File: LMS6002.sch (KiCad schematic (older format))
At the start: 40 parts, among them J1 SMA_H, J2 SMA_H, T1 B0322J5050, T2 B0322J5050, U3 LMS6002DR2

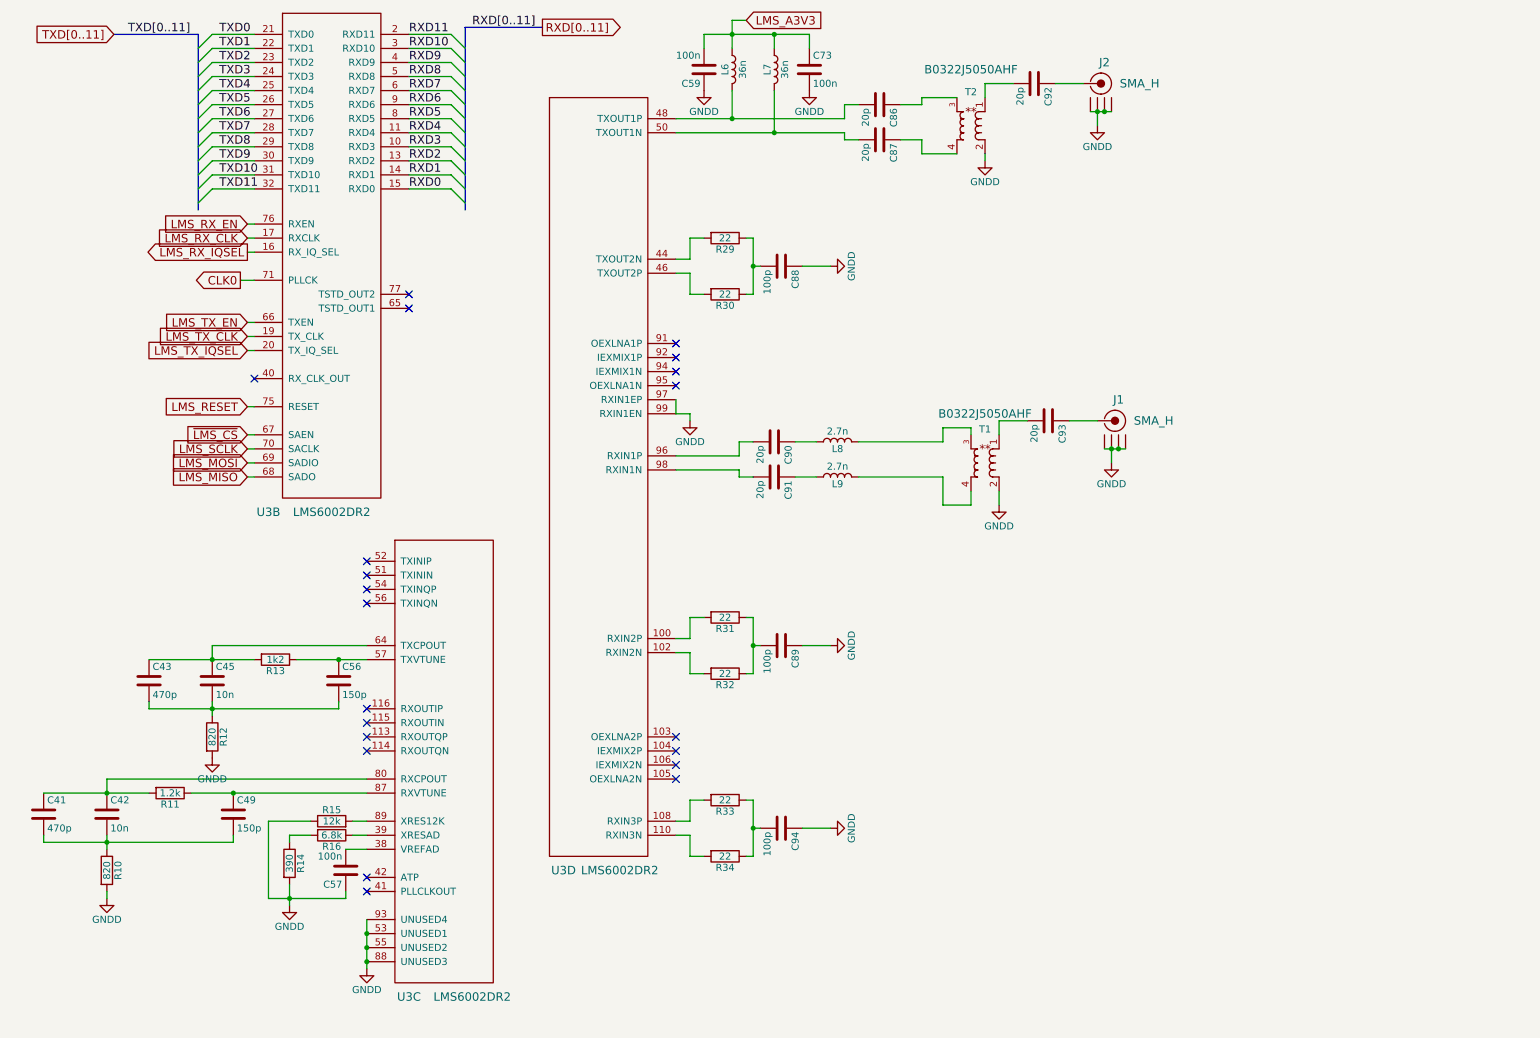
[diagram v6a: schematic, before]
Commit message: Changed RF sheet to add second path to TX and RX
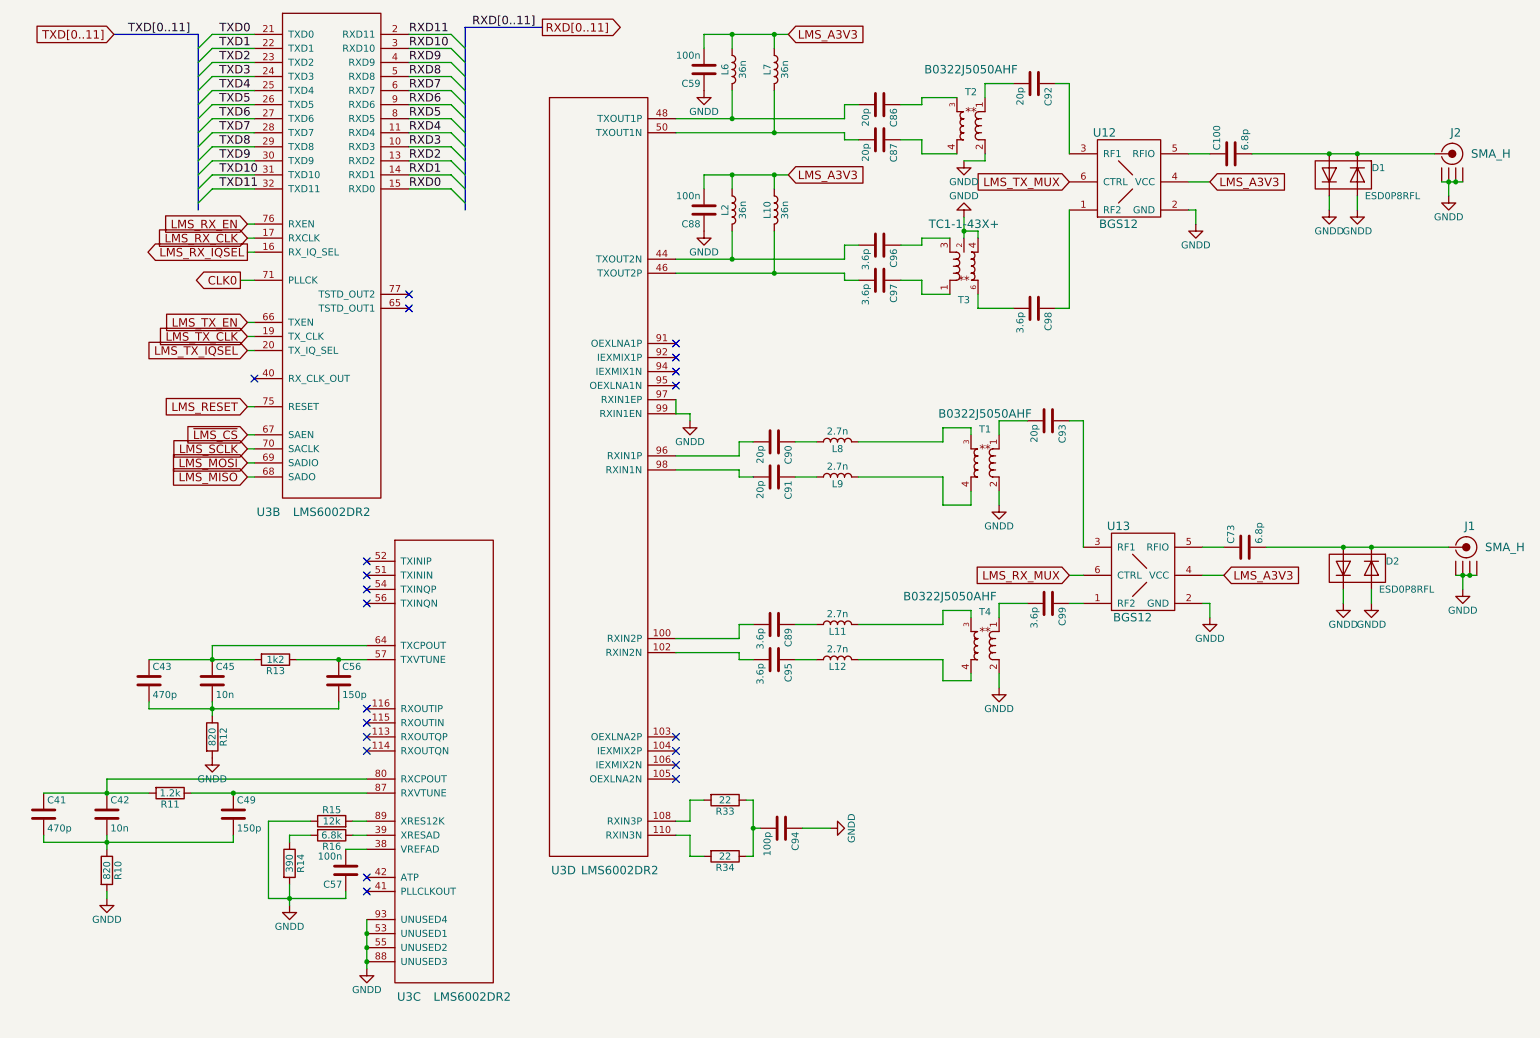
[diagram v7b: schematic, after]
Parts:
- removed R29, R30, R31, R32: 22, Resistors_SMD:R_0603, symbol R
- added C100: 6.8p, Capacitors_SMD:C_0603, symbol C
- added C95, C96, C97, C98, C99: 3.6p, Capacitors_SMD:C_0603, symbol C
- added D1, D2: ESD0P8RFL, sdr-foots:TSLP-4-7, symbol DualDiode
- added L10, L2: 36n, Inductors_SMD:L_0603, symbol L
- added L11, L12: 2.7n, Inductors_SMD:L_0603, symbol L
- added T3: TR_TC1-1-43X+, sdr-foots:TC1-1-43X+, symbol TR_TC1-1-43X+
- added T4: B0322J5050, sdr-foots:B0322J5050, symbol B0322J5050
- added U12, U13: BGS12, sdr-foots:TSLP-6-4, symbol BGS12
- C73: value 100n -> 6.8p
- C88: value 100p -> 100n
- C89: value 100p -> 3.6p
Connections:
- net GNDD: now also D1.2 (A), D1.3 (K), D1.4 (A), D2.2 (A), D2.3 (K), D2.4 (A), T3.2, T3.4, T4.2 (GND), U12.2 (GND), U13.2 (GND); no longer C73.2, C89.1
- net LMS_A3V3: now also C88.2, L10.1, L2.1, U12.4 (VCC), U13.4 (VCC); no longer C73.1
- net at U3.100 (RXIN2P): now also C89.2
- net at U3.102 (RXIN2N): now also C95.2
- net at U3.44 (TXOUT2N): now also C96.2, L2.2
- net at U3.46 (TXOUT2P): now also C97.2, L10.2
- net at C93.1: now also U13.3 (RF1); no longer J1.1 (RF)
- net at J2.1 (RF): now also C100.2, D1.1 (K), D1.4 (A); no longer C92.1
- new net: C92.1, U12.3 (RF1)
- new net: C98.1, U12.1 (RF2)
- new net: C100.1, U12.5 (RFIO)
- new net: C97.1, T3.1
- new net: C96.1, T3.3
- new net: C98.2, T3.6
- new net: C73.2, D2.1 (K), D2.4 (A), J1.1 (RF)
- new net: C99.1, U13.1 (RF2)
- new net: C73.1, U13.5 (RFIO)
- new net: C95.1, L12.1
- new net: C89.1, L11.1
- new net: L11.2, T4.3
- new net: L12.2, T4.4
- new net: C99.2, T4.1
- new net LMS_RX_MUX: U13.6 (CTRL)
- new net LMS_TX_MUX: U12.6 (CTRL)
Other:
- moved on the sheet: J2

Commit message: Small changes
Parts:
- removed T4: B0322J5050, sdr-foots:B0322J5050, symbol B0322J5050
- added T4: TR_TC1-1-43X+, sdr-foots:TC1-1-43X+, symbol TR_TC1-1-43X+
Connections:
- net GNDD: now also T4.2, T4.6
- net at L11.2: now also T4.3
- net at L12.2: now also T4.1
- net at C99.2: now also T4.4
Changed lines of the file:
@@
 $EndComp
 $Comp
-L GNDD #PWR42
+L GNDD #PWR039
 U 1 1 58A337CD
 P 3000 7400
-F 0 "#PWR42" H 3000 7150 50  0001 C CNN
+F 0 "#PWR039" H 3000 7150 50  0001 C CNN
 F 1 "GNDD" H 3000 7250 50  0000 C CNN
 F 2 "" H 3000 7400 50  0000 C CNN
@@
 NoConn ~ 3000 4500
 $Comp
-L GNDD #PWR39
+L GNDD #PWR040
 U 1 1 58A3826F
 P 1150 6900
-F 0 "#PWR39" H 1150 6650 50  0001 C CNN
+F 0 "#PWR040" H 1150 6650 50  0001 C CNN
 F 1 "GNDD" H 1150 6750 50  0000 C CNN
 F 2 "" H 1150 6900 50  0000 C CNN
@@
 $EndComp
 $Comp
-L GNDD #PWR40
+L GNDD #PWR041
 U 1 1 58A38F2B
 P 1900 5900
-F 0 "#PWR40" H 1900 5650 50  0001 C CNN
+F 0 "#PWR041" H 1900 5650 50  0001 C CNN
 F 1 "GNDD" H 1900 5750 50  0000 C CNN
 F 2 "" H 1900 5900 50  0000 C CNN
@@
 $EndComp
 $Comp
-L GNDD #PWR41
+L GNDD #PWR042
 U 1 1 58A3A1AF
 P 2450 6950
-F 0 "#PWR41" H 2450 6700 50  0001 C CNN
+F 0 "#PWR042" H 2450 6700 50  0001 C CNN
 F 1 "GNDD" H 2450 6800 50  0000 C CNN
 F 2 "" H 2450 6950 50  0000 C CNN
@@
 LMS_A3V3
 $Comp
-L GNDD #PWR44
+L GNDD #PWR043
 U 1 1 58C78FD2
 P 5400 1150
-F 0 "#PWR44" H 5400 900 50  0001 C CNN
+F 0 "#PWR043" H 5400 900 50  0001 C CNN
 F 1 "GNDD" H 5400 1000 50  0000 C CNN
 F 2 "" H 5400 1150 50  0001 C CNN
@@
 $EndComp
 $Comp
-L GNDD #PWR47
+L GNDD #PWR044
 U 1 1 58CD0D99
 P 7250 1650
-F 0 "#PWR47" H 7250 1400 50  0001 C CNN
+F 0 "#PWR044" H 7250 1400 50  0001 C CNN
 F 1 "GNDD" H 7250 1500 50  0000 C CNN
 F 2 "" H 7250 1650 50  0001 C CNN
@@
 $EndComp
 $Comp
-L GNDD #PWR57
+L GNDD #PWR045
 U 1 1 58CD131D
 P 10700 1900
-F 0 "#PWR57" H 10700 1650 50  0001 C CNN
+F 0 "#PWR045" H 10700 1650 50  0001 C CNN
 F 1 "GNDD" H 10700 1750 50  0000 C CNN
 F 2 "" H 10700 1900 50  0001 C CNN
@@
 $EndComp
 $Comp
-L GNDD #PWR49
+L GNDD #PWR046
 U 1 1 58CD22F1
 P 7500 4100
-F 0 "#PWR49" H 7500 3850 50  0001 C CNN
+F 0 "#PWR046" H 7500 3850 50  0001 C CNN
 F 1 "GNDD" H 7500 3950 50  0000 C CNN
 F 2 "" H 7500 4100 50  0001 C CNN
@@
 $EndComp
 $Comp
-L GNDD #PWR43
+L GNDD #PWR047
 U 1 1 58CD4F1D
 P 5300 3500
-F 0 "#PWR43" H 5300 3250 50  0001 C CNN
+F 0 "#PWR047" H 5300 3250 50  0001 C CNN
 F 1 "GNDD" H 5300 3350 50  0000 C CNN
 F 2 "" H 5300 3500 50  0001 C CNN
@@
 $EndComp
 $Comp
-L GNDD #PWR46
+L GNDD #PWR048
 U 1 1 58CD63CB
 P 6300 6400
-F 0 "#PWR46" H 6300 6150 50  0001 C CNN
+F 0 "#PWR048" H 6300 6150 50  0001 C CNN
 F 1 "GNDD" H 6300 6250 50  0000 C CNN
 F 2 "" H 6300 6400 50  0001 C CNN
@@
 LMS_A3V3
 $Comp
-L GNDD #PWR45
+L GNDD #PWR049
 U 1 1 5923BA82
 P 5400 2150
-F 0 "#PWR45" H 5400 1900 50  0001 C CNN
+F 0 "#PWR049" H 5400 1900 50  0001 C CNN
 F 1 "GNDD" H 5400 2000 50  0000 C CNN
 F 2 "" H 5400 2150 50  0001 C CNN
@@
 $EndComp
 $Comp
-L GNDD #PWR48
+L GNDD #PWR050
 U 1 1 5923C1B8
 P 7250 2050
-F 0 "#PWR48" H 7250 1800 50  0001 C CNN
+F 0 "#PWR050" H 7250 1800 50  0001 C CNN
 F 1 "GNDD" H 7250 1900 50  0000 C CNN
 F 2 "" H 7250 2050 50  0001 C CNN
@@
 $EndComp
 $Comp
-L GNDD #PWR51
+L GNDD #PWR051
 U 1 1 5923D614
 P 8900 2100
-F 0 "#PWR51" H 8900 1850 50  0001 C CNN
+F 0 "#PWR051" H 8900 1850 50  0001 C CNN
 F 1 "GNDD" H 8900 1950 50  0000 C CNN
 F 2 "" H 8900 2100 50  0001 C CNN
@@
 $EndComp
 $Comp
-L GNDD #PWR53
+L GNDD #PWR052
 U 1 1 59242BC0
 P 9850 2000
-F 0 "#PWR53" H 9850 1750 50  0001 C CNN
+F 0 "#PWR052" H 9850 1750 50  0001 C CNN
 F 1 "GNDD" H 9850 1850 50  0000 C CNN
 F 2 "" H 9850 2000 50  0001 C CNN
@@
 $EndComp
 $Comp
-L GNDD #PWR55
+L GNDD #PWR053
 U 1 1 59242C5B
 P 10050 2000
-F 0 "#PWR55" H 10050 1750 50  0001 C CNN
+F 0 "#PWR053" H 10050 1750 50  0001 C CNN
 F 1 "GNDD" H 10050 1850 50  0000 C CNN
 F 2 "" H 10050 2000 50  0001 C CNN
@@
 $EndComp
 $Comp
-L GNDD #PWR58
+L GNDD #PWR054
 U 1 1 5924388E
 P 10800 4700
-F 0 "#PWR58" H 10800 4450 50  0001 C CNN
+F 0 "#PWR054" H 10800 4450 50  0001 C CNN
 F 1 "GNDD" H 10800 4550 50  0000 C CNN
 F 2 "" H 10800 4700 50  0001 C CNN
@@
 $EndComp
 $Comp
-L GNDD #PWR52
+L GNDD #PWR055
 U 1 1 5924389A
 P 9000 4900
-F 0 "#PWR52" H 9000 4650 50  0001 C CNN
+F 0 "#PWR055" H 9000 4650 50  0001 C CNN
 F 1 "GNDD" H 9000 4750 50  0000 C CNN
 F 2 "" H 9000 4900 50  0001 C CNN
@@
 $EndComp
 $Comp
-L GNDD #PWR54
+L GNDD #PWR056
 U 1 1 592438B8
 P 9950 4800
-F 0 "#PWR54" H 9950 4550 50  0001 C CNN
+F 0 "#PWR056" H 9950 4550 50  0001 C CNN
 F 1 "GNDD" H 9950 4650 50  0000 C CNN
 F 2 "" H 9950 4800 50  0001 C CNN
@@
 $EndComp
 $Comp
-L GNDD #PWR56
+L GNDD #PWR057
 U 1 1 592438BE
 P 10150 4800
-F 0 "#PWR56" H 10150 4550 50  0001 C CNN
+F 0 "#PWR057" H 10150 4550 50  0001 C CNN
 F 1 "GNDD" H 10150 4650 50  0000 C CNN
 F 2 "" H 10150 4800 50  0001 C CNN
@@
 $EndComp
 $Comp
-L B0322J5050 T4
-U 1 1 59244E97
-P 7400 5100
-F 0 "T4" H 7400 5340 50  0000 C CNN
-F 1 "B0322J5050" H 7400 5475 50  0001 C CNN
-F 2 "sdr-foots:B0322J5050" H 7425 5575 60  0001 C CNN
-F 3 "" H 7400 5340 60  0001 C CNN
-F 4 "Anaren" H 7450 5925 60  0001 C CNN "Manufacturer"
-F 5 "RF_Transformer;300_-_3000_MHz;_RF_Power_2_Watt;_Ratio_1:1;_50_Ohm;" H 7625 5700 60  0001 C CNN "Description"
-F 6 "B0322J5050AHF" H 7150 5450 60  0000 C CNN "Vendor Part Number"
-F 7 "B0322J5050" H 7400 4800 60  0001 C CNN "Component Value"
-	1    7400 5100
-	1    0    0    -1
-$EndComp
-$Comp
 L C C99
 U 1 1 592451B5
@@
 $EndComp
 $Comp
-L GNDD #PWR50
+L GNDD #PWR058
 U 1 1 5924556E
 P 7500 5400
-F 0 "#PWR50" H 7500 5150 50  0001 C CNN
+F 0 "#PWR058" H 7500 5150 50  0001 C CNN
 F 1 "GNDD" H 7500 5250 50  0000 C CNN
 F 2 "" H 7500 5400 50  0001 C CNN
@@
 Wire Wire Line
 	7500 5400 7500 5300
+$Comp
+L TR_TC1-1-43X+ T4
+U 1 1 59246EFC
+P 7400 5100
+F 0 "T4" H 7400 5340 50  0000 C CNN
+F 1 "TR_TC1-1-43X+" H 7400 5475 50  0001 C CNN
+F 2 "sdr-foots:TC1-1-43X+" H 7425 5575 60  0001 C CNN
+F 3 "" H 7400 5340 60  0000 C CNN
+F 4 "Mini-Circuits" H 7450 5925 60  0001 C CNN "Manufacturer"
+F 5 "RF_Transformer;_650_-_4000_MHz;_RF_Power_0.25_Watt;_Ratio_1:1;_50_Ohm;" H 7625 5700 60  0001 C CNN "Description"
+F 6 "TC1-1-43X+" H 7525 5825 60  0001 C CNN "Manufacturer Part Number"
+F 7 "TC1-1-43X+" H 7450 6150 60  0001 C CNN "Vendor Part Number"
+F 8 "TC1-1-43X+" H 7800 4800 60  0000 C CNN "Component Value"
+	1    7400 5100
+	-1   0    0    1
+$EndComp
+$Comp
+L GNDD #PWR059
+U 1 1 59247241
+P 7400 4850
+F 0 "#PWR059" H 7400 4600 50  0001 C CNN
+F 1 "GNDD" H 7400 4700 50  0000 C CNN
+F 2 "" H 7400 4850 50  0001 C CNN
+F 3 "" H 7400 4850 50  0001 C CNN
+	1    7400 4850
+	-1   0    0    1
+$EndComp
+Wire Wire Line
+	7400 4900 7400 4850
 $EndSCHEMATC
